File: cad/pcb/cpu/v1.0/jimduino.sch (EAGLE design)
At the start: 37 parts, among them P1 DF12-32-DP, P2 DF12-32-DP, Q1 FDN360P, SW1 ON/OFF, U1 STM32F415R, U2 MCP1703, U4 LTC2954-2, Y1 8Y-16.000MAAV-T, Y2 16MHz

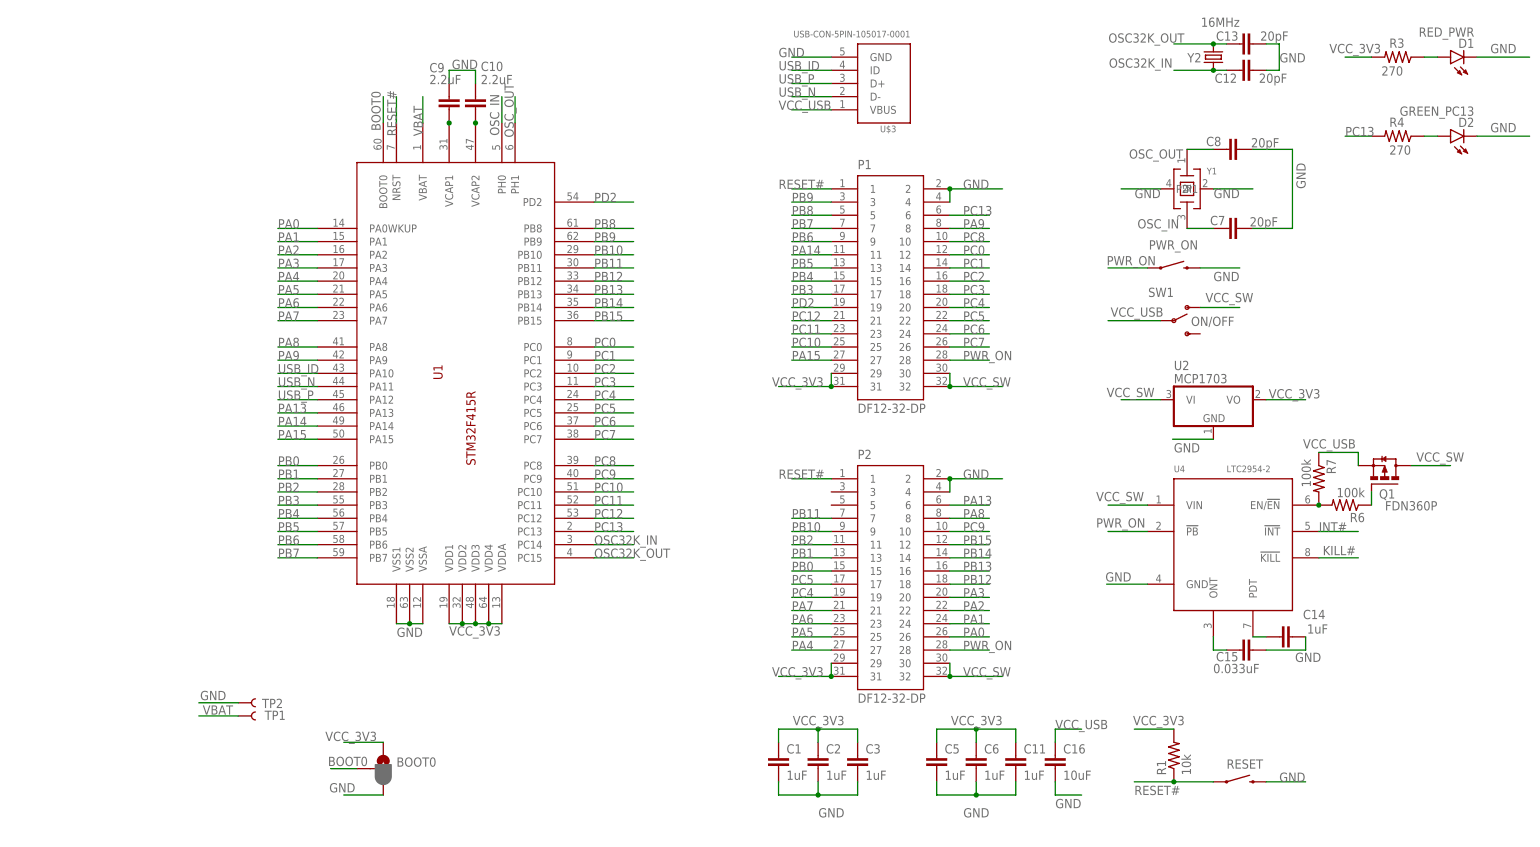
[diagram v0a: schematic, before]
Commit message: Move components and switches around.
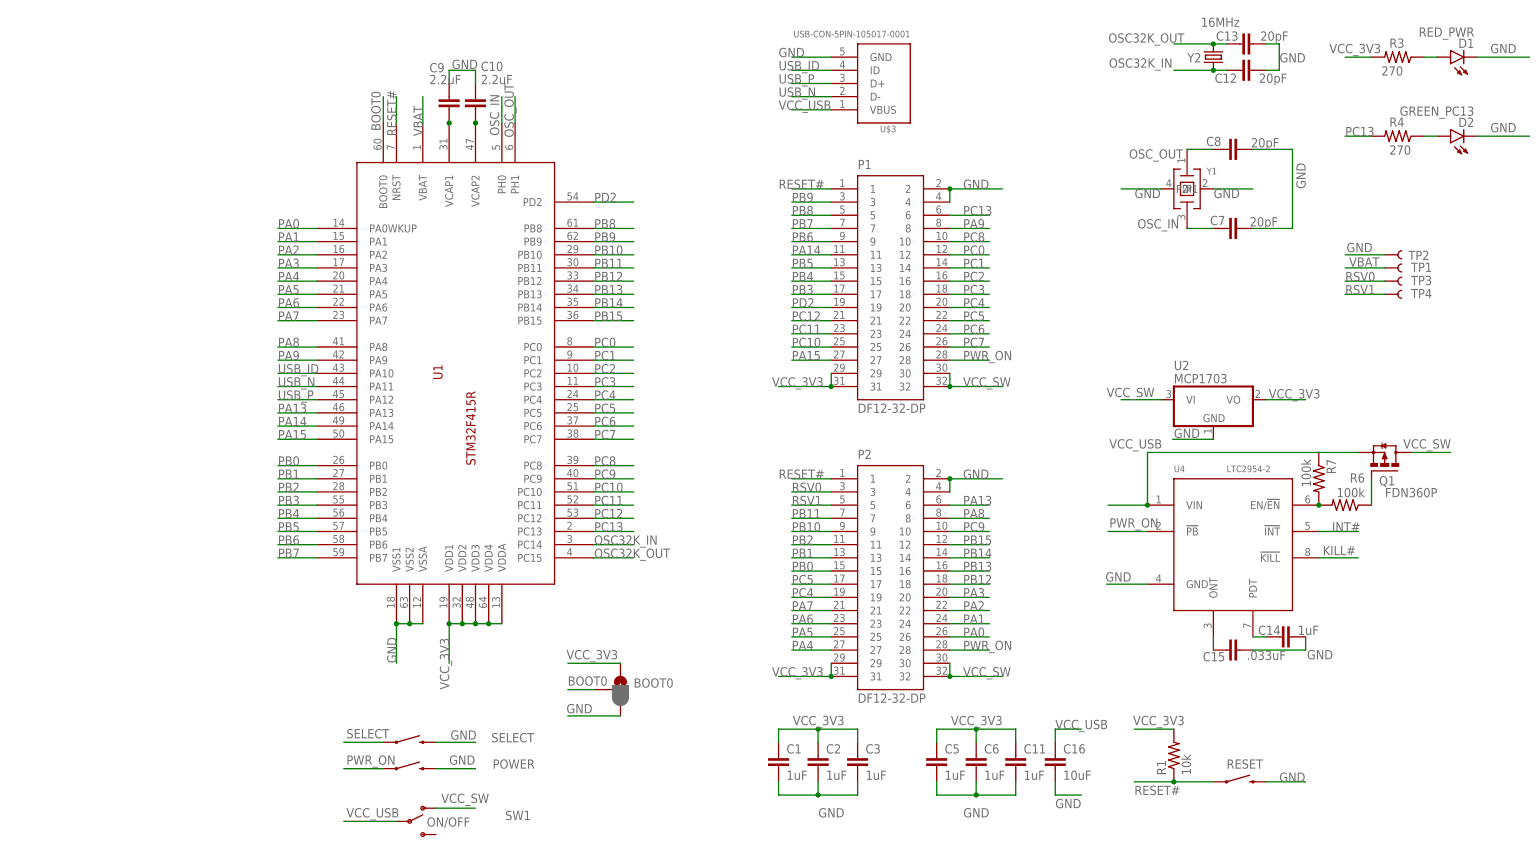
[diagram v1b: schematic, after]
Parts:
- removed PWR_ON: SWITCH-MOMENTARY-2SMD-REDUNDANT, SparkFun-Electromechanical:SWITCH-MOMENTARY-2SMD-REDUNDANT
- added POWER, SELECT: SWITCH-MOMENTARY-2SMD-REDUNDANT, SparkFun-Electromechanical:SWITCH-MOMENTARY-2SMD-REDUNDANT
- added TP3, TP4: TEST-POINT3, SparkFun-Passives:TEST-POINT3
- C15: value 0.033uF -> .033uF
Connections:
- new net RSV0: P2.3, TP3.1
- new net RSV1: P2.5, TP4.1
- new net SELECT: SELECT.1
- net GND: now also POWER.2, SELECT.2; no longer PWR_ON.2
- net PWR_ON: now also POWER.1; no longer PWR_ON.1
- net VCC_SW: no longer U4.VIN
- net VCC_USB: now also U4.VIN
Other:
- moved on the sheet: BOOT0, C15, Q1, SW1, TP1, TP2

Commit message: Add LIPO charging circuit.
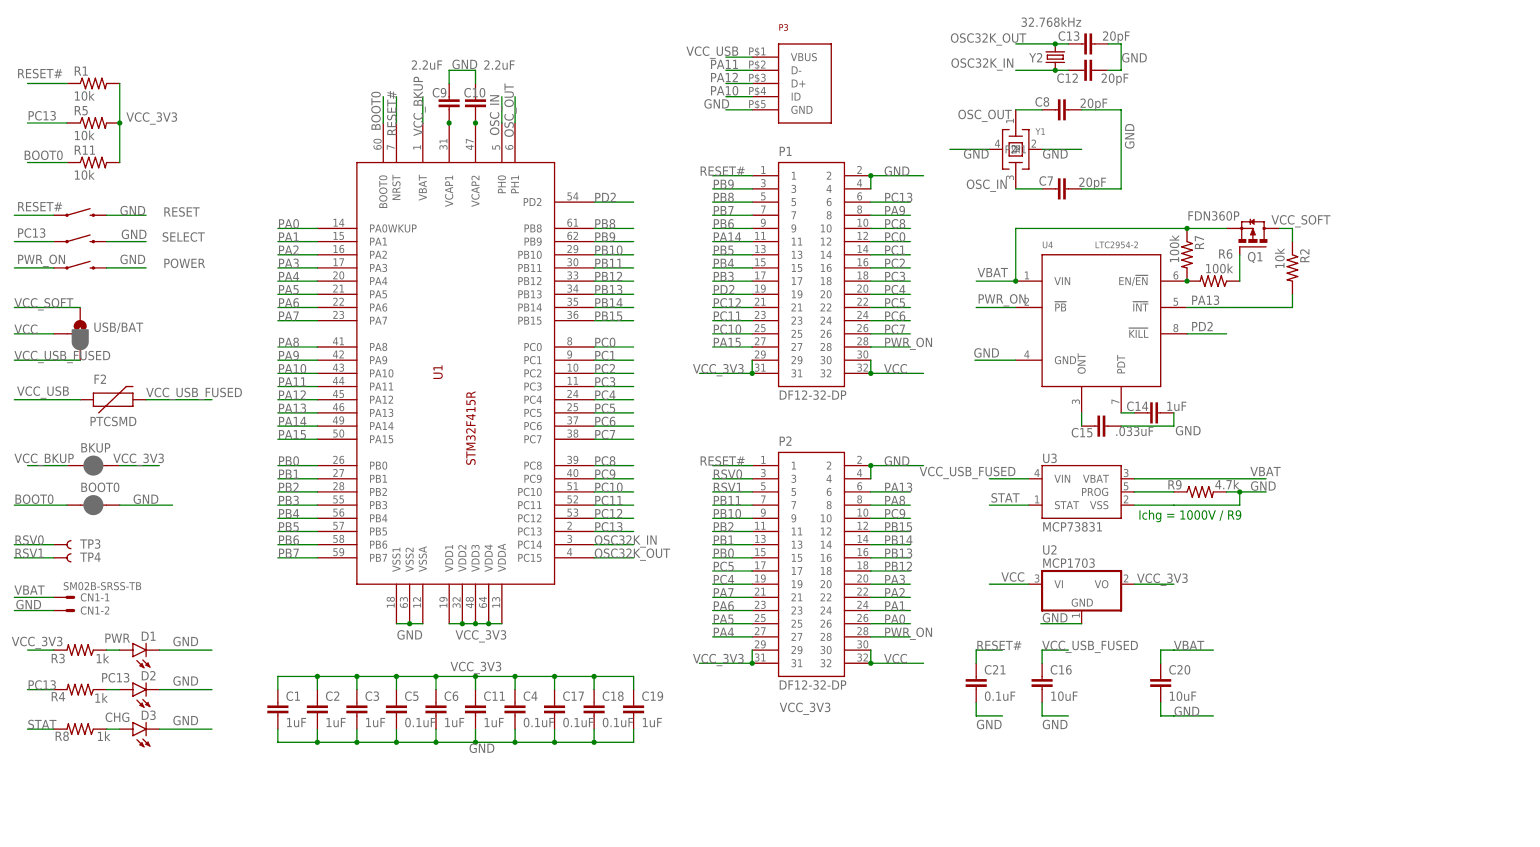
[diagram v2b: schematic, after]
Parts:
- removed SW1: ON/OFF, SparkFun-Electromechanical:SWITCH-SPDTSMD2
- removed TP1, TP2: TEST-POINT3, SparkFun-Passives:TEST-POINT3
- removed U$3: USB-CON-5PIN-105017-0001, GeekAmmo:USB-CON-5PIN-105017-0001
- added BKUP: JUMPER-PAD-2-NC_BY_PASTE, SparkFun-Passives:JUMPER-PAD-2-NC_BY_PASTE
- added C17, C18, C21, C4: 0.1uF, SparkFun-Capacitors:CAP0805
- added C19: 1uF, SparkFun-Capacitors:CAP0805
- added C20: 10uF, SparkFun-Capacitors:CAP0805
- added CN1: SM02B-SRSS-TB, con-jst2:SM02B-SRSS-TB
- added D3: CHG, SparkFun-LED:LED0603
- added F2: PTCSMD, SparkFun-PowerIC:PTCSMD
- added P3: MICROUSB, jimduino:MICROUSB
- added R11, R2, R5: 10k, SparkFun-Passives:RESISTOR0805-RES
- added R8: 1k, SparkFun-Passives:RESISTOR0805-RES
- added R9: 4.7k, SparkFun-Passives:RESISTOR0805-RES
- added U3: MCP73831, SparkFun-PowerIC:MCP73831
- added USB/BAT: JUMPER-PAD-3-2OF3_NC_BY_PASTE, SparkFun-Passives:JUMPER-PAD-3-2OF3_NC_BY_PASTE
- BOOT0: value JUMPER-PAD-3-2OF3_NC_BY_PASTE -> JUMPER-PAD-2-NC_BY_PASTE; device SparkFun-Passives:JUMPER-PAD-3-2OF3_NC_BY_PASTE -> SparkFun-Passives:JUMPER-PAD-2-NC_BY_PASTE
- C5: value 1uF -> 0.1uF
- D1: value RED_PWR -> PWR
- D2: value GREEN_PC13 -> PC13
- R1: device SparkFun-Passives:RESISTOR0402-RES -> SparkFun-Passives:RESISTOR0805-RES
- R3, R4: value 270 -> 1k
- Y2: value 16MHz -> 32.768kHz
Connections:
- removed net INT#: U4.!INT!
- removed net KILL#: U4.!KILL!
- removed net SELECT: SELECT.1
- removed net USB_ID: U$3.ID, U1.PA10
- removed net USB_N: U$3.D-, U1.PA11
- removed net USB_P: U$3.D+, U1.PA12
- removed net VCC_SW: P1.30, P1.32, P2.30, P2.32, Q1.D, SW1.O, U2.VI
- new net N$10: D3.A, R8.1
- new net N$11: R9.1, U3.PROG
- new net PA10: P3.ID, U1.PA10
- new net PA11: P3.D-, U1.PA11
- new net PA12: P3.D+, U1.PA12
- new net STAT: R8.2, U3.STAT
- new net VCC: P1.30, P1.32, P2.30, P2.32, U2.VI, USB/BAT.2
- new net VCC_BKUP: BKUP.1, U1.VBAT
- new net VCC_SOFT: Q1.D, R2.1, USB/BAT.1
- new net VCC_USB_FUSED: C16.1, F2.2, U3.VIN, USB/BAT.3
- net BOOT0: now also BOOT0.1, R11.1; no longer BOOT0.2
- net GND: now also BOOT0.2, C17.2, C18.2, C19.2, C20.2, C21.2, C4.2, CN1-2.S, D3.C, P3.GND, R9.2, U3.VSS; no longer BOOT0.3, TP2.1, U$3.GND
- net PA13: now also R2.2, U4.!INT!
- net PC13: now also R5.1, SELECT.1
- net PD2: now also U4.!KILL!
- net RESET#: now also C21.1
- net VBAT: now also C20.1, CN1-1.S, Q1.S, R7.1, U3.VBAT, U4.VIN; no longer TP1.1, U1.VBAT
- net VCC_3V3: now also BKUP.2, C17.1, C18.1, C19.1, C4.1, R11.2, R5.2; no longer BOOT0.1
- net VCC_USB: now also F2.1, P3.VBUS; no longer C16.1, Q1.S, R7.1, SW1.P, U$3.VBUS, U4.VIN
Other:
- note added: "Ichg = 1000V / R9"
- moved on the sheet: C1, C11, C12, C13, C14, C15, C16, C2, C3, C5, C6, C7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

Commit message: Add more intelligent power switching and improve schematic layout.
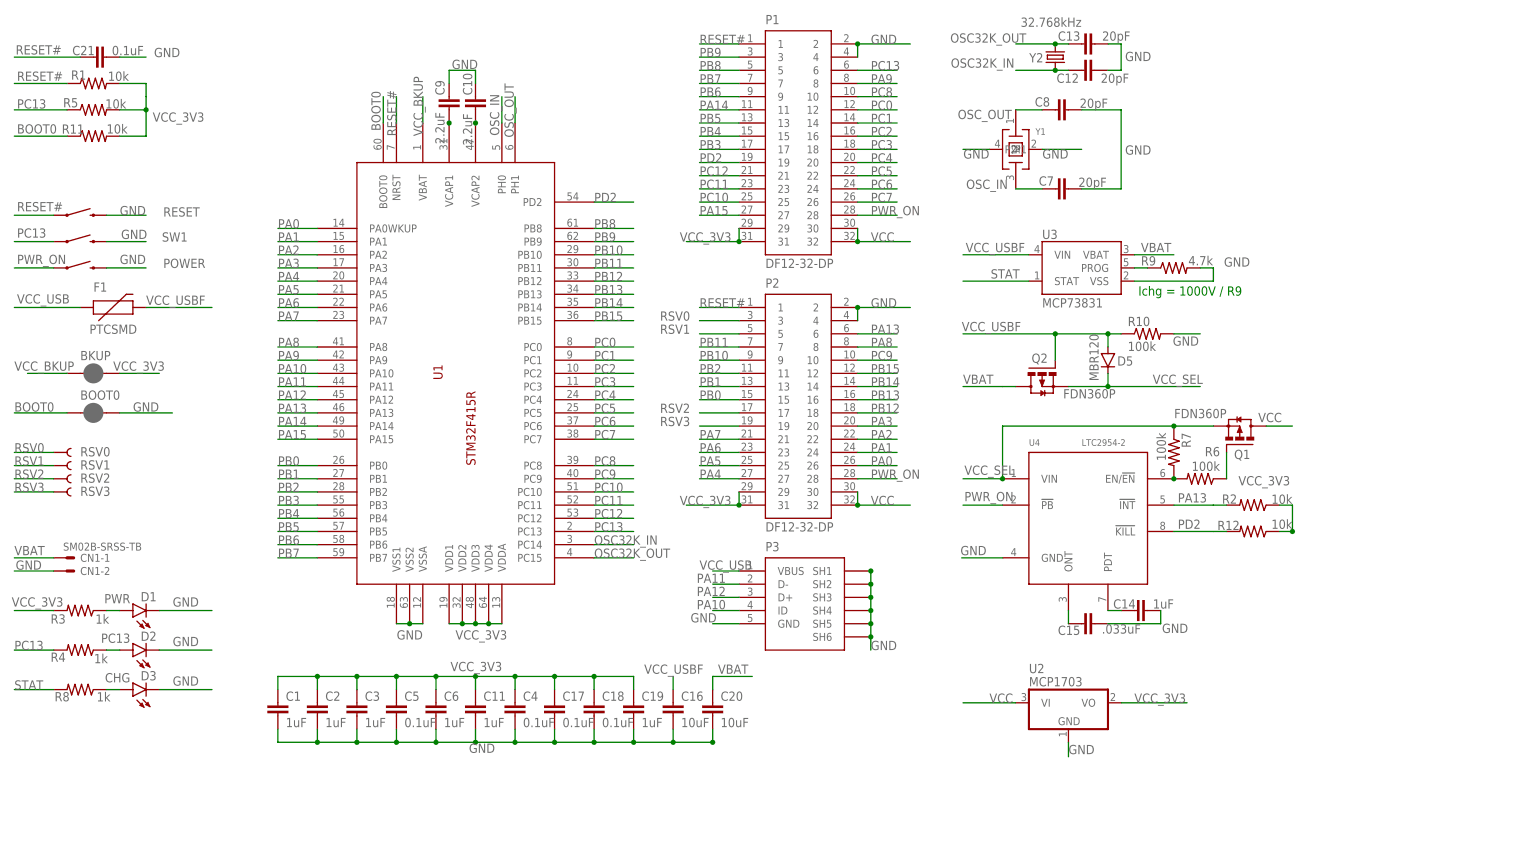
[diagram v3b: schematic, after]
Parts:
- removed F2: PTCSMD, SparkFun-PowerIC:PTCSMD
- removed TP3, TP4: TEST-POINT3, SparkFun-Passives:TEST-POINT3
- removed USB/BAT: JUMPER-PAD-3-2OF3_NC_BY_PASTE, SparkFun-Passives:JUMPER-PAD-3-2OF3_NC_BY_PASTE
- added D5: MBR120, SparkFun-DiscreteSemi:DIODESOD123
- added F1: PTCSMD, SparkFun-PowerIC:PTCSMD
- added Q2: FDN360P, transistor-power:FDN360P
- added R10: 100k, SparkFun-Passives:RESISTOR0805-RES
- added R12: 10k, SparkFun-Passives:RESISTOR0805-RES
- added RSV0, RSV1, RSV2, RSV3: TEST-POINT3, SparkFun-Passives:TEST-POINT3
- renumbered SELECT to SW1
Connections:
- removed net VCC_SOFT: Q1.D, R2.1, USB/BAT.1
- removed net VCC_USB_FUSED: C16.1, F2.2, U3.VIN, USB/BAT.3
- new net RSV2: P2.17, RSV2.1
- new net RSV3: P2.19, RSV3.1
- new net VCC_SEL: D5.C, Q1.S, Q2.S, R7.1, U4.VIN
- new net VCC_USBF: C16.1, D5.A, F1.2, Q2.G, R10.1, U3.VIN
- net GND: now also P3.SH1, P3.SH2, P3.SH3, P3.SH4, P3.SH5, P3.SH6, R10.2
- net PC4: no longer P2.19
- net PC5: no longer P2.17
- net PD2: now also R12.2
- net RSV0: now also RSV0.1; no longer TP3.1
- net RSV1: now also RSV1.1; no longer TP4.1
- net VBAT: now also Q2.D; no longer Q1.S, R7.1, U4.VIN
- net VCC: now also Q1.D; no longer USB/BAT.2
- net VCC_3V3: now also R12.1, R2.1
- net VCC_USB: now also F1.1; no longer F2.1
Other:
- moved on the sheet: BKUP, BOOT0, C14, C15, C16, C20, C21, CN1-1, CN1-2, D1, D2, D3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

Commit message: Release candidate 0
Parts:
- BKUP, BOOT0, C1, C10, C11, C12, C13, C14, C15, C16, C17, C18, C19, C2, C20, C21, C3, C4, C5, C6, C9, CN1, D1, D2, D3, D5, F1, P1, P2, P3, POWER, Q1, Q2, R1, R10, R11, R12, R2, R3, R4, R5, R6, R7, R8, R9, RESET, RSV0, RSV1, RSV2, RSV3, SW1, U1, U2, U3, U4, Y1, Y2: OC_NEWARK (none) -> unknown
- C7, C8: value 20pF -> 22pF; OC_NEWARK (none) -> unknown

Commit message: Release Candidate 1
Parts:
- BKUP, BOOT0, C1, C10, C11, C12, C13, C14, C15, C16, C17, C18, C19, C2, C20, C21, C3, C4, C5, C6, C9, CN1, D1, D2, D3, D5, F1, P1, P2, P3, POWER, Q1, Q2, R1, R10, R11, R12, R2, R3, R4, R5, R6, R7, R8, R9, RESET, RSV0, RSV1, RSV2, RSV3, SW1, U1, U2, U3, U4, Y1, Y2: OC_NEWARK unknown -> (none)
- C7, C8: value 22pF -> 20pF; OC_NEWARK unknown -> (none)

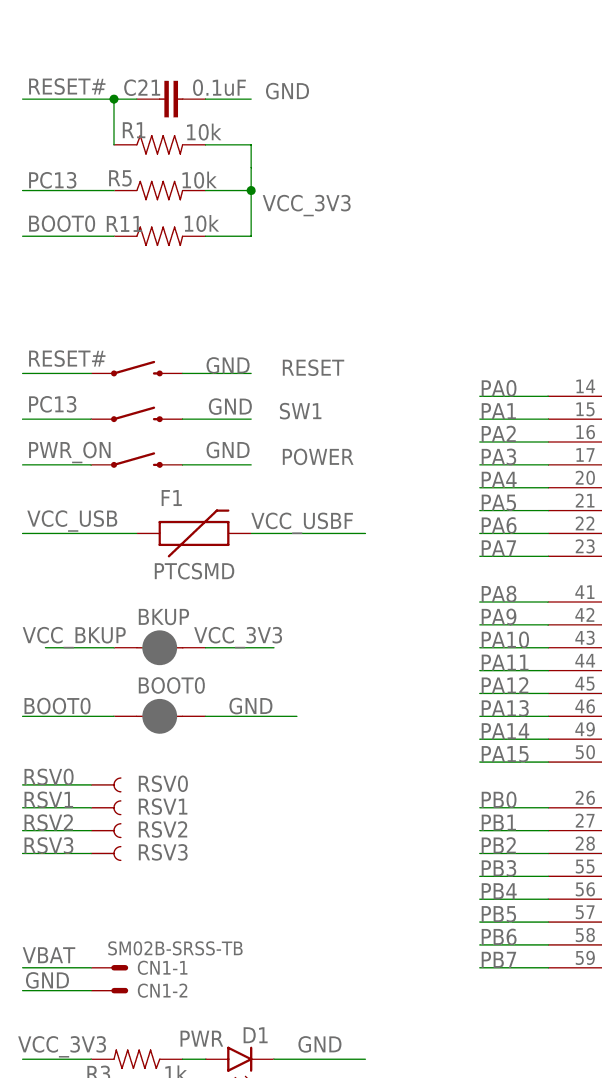
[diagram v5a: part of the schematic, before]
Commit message: Switch to 0402 capacitors
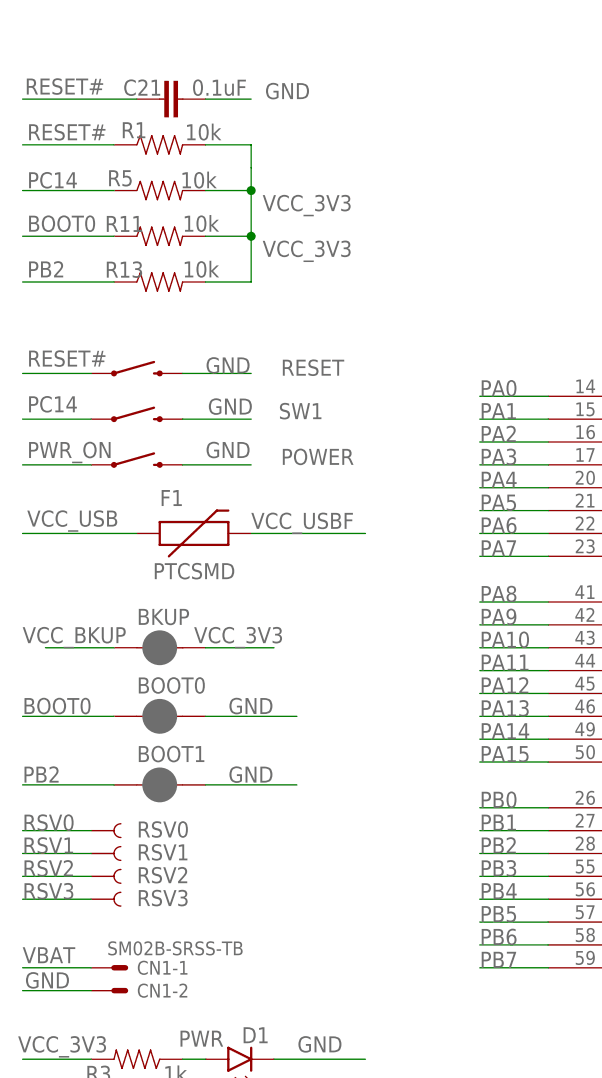
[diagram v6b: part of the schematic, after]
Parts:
- added BOOT1: JUMPER-PAD-2-NC_BY_PASTE, SparkFun-Passives:JUMPER-PAD-2-NC_BY_PASTE
- added R13: 10k, SparkFun-Passives:RESISTOR0402-RES
- C1, C10, C11, C12, C13, C14, C15, C17, C18, C19, C2, C21, C3, C4, C5, C6, C7, C8, C9: device SparkFun-Capacitors:CAP0805 -> SparkFun-Capacitors:CAP0402-CAP
- R1, R10, R11, R12, R2, R3, R4, R5, R6, R7, R8, R9: device SparkFun-Passives:RESISTOR0805-RES -> SparkFun-Passives:RESISTOR0402-RES
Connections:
- new net PC14: R5.1, SW1.1
- net GND: now also BOOT1.2
- net PB2: now also BOOT1.1, R13.1
- net PC13: no longer R5.1, SW1.1
- net VCC_3V3: now also R13.2
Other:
- moved on the sheet: RSV0, RSV1, RSV2, RSV3

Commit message: Release Candidate 2
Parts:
- BOOT0, BOOT1: value JUMPER-PAD-2-NC_BY_PASTE -> JUMPER-PAD-2-NOYES_SILK; device SparkFun-Passives:JUMPER-PAD-2-NC_BY_PASTE -> SparkFun-Passives:JUMPER-PAD-2-NOYES_SILK
- C1, C10, C11, C14, C15, C17, C18, C19, C2, C21, C3, C4, C5, C6, C9: device SparkFun-Capacitors:CAP0402-CAP -> SparkFun-Capacitors:CAP0805
- C12, C13: value 20pF -> 4pF
- C7, C8: value 20pF -> 4pF; device SparkFun-Capacitors:CAP0402-CAP -> SparkFun-Capacitors:CAP0805
- D2: value PC13 -> BOOT1
- R1, R10, R11, R12, R13, R2, R3, R4, R5, R6, R7, R8, R9: device SparkFun-Passives:RESISTOR0402-RES -> SparkFun-Passives:RESISTOR0805-RES
- Y1: value 8Y-16.000MAAV-T -> 16MHz(9pF)
- Y2: value 32.768kHz -> 32.768kHz (9pF)
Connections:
- removed net PC14: R5.1, SW1.1
- net GND: now also R11.2, R13.2; no longer BOOT0.2, BOOT1.2
- net PB2: now also R4.2
- net PC13: now also R5.1, SW1.1; no longer R4.2
- net VCC_3V3: now also BOOT0.2, BOOT1.2; no longer R11.2, R13.2
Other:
- moved on the sheet: RSV0, RSV1, RSV2, RSV3
